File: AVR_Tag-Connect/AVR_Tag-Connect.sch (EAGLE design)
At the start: 17 parts, among them J1 MF-CON-2.54mm-01x10, J2 MF-CON-2.54mm-01x10, U1 ATMEGA328P-AU, X1 ABMM-16.000MHZ-B2-T

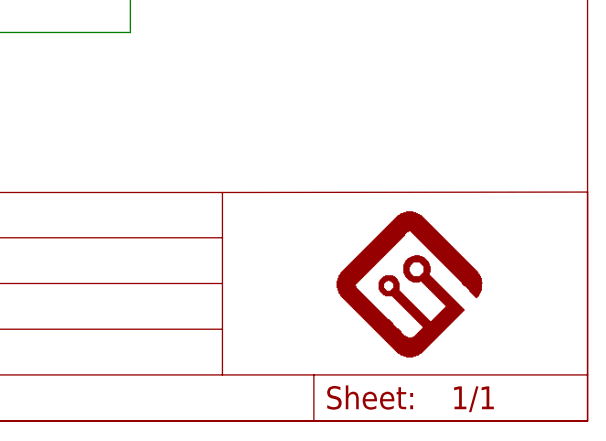
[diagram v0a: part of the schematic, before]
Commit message: Updated to recent library changes.
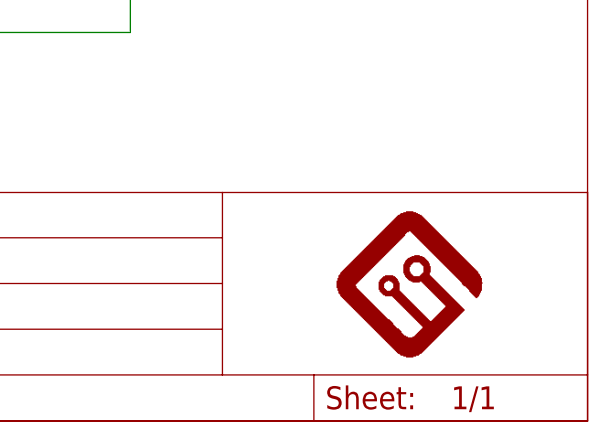
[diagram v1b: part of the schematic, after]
